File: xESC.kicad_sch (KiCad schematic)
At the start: 48 parts, among them J22 Screw_Terminal_01x03, J36 Conn_02x03_Odd_Even, J39 Screw_Terminal_01x02, J42 Conn_01x02, J45 67800-8005, J48 Conn_01x05, U10 xESC2, U20 2.54mm 2x2 socket, U23 2.54mm 2x2 socket, U26 2.54mm 2x2 socket, U28 LV2862XDDC, U32 2.54mm 1x6 socket, U35 2.54mm 1x6 socket, U38 2.54mm 1x9 socket, U41 2.54mm 1x5 socket

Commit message: Updated to the non-pcb mount xt30 connectors
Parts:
- J42: footprint Connector_AMASS:AMASS_XT30UPB-M_1x02_P5.0mm_Vertical -> Connector_AMASS:AMASS_XT30U-M_1x02_P5.0mm_Vertical; JLC C428721 -> C99101
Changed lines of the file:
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@@
 			)
 		)
-		(property "Footprint" "Connector_AMASS:AMASS_XT30UPB-M_1x02_P5.0mm_Vertical"
+		(property "Footprint" "Connector_AMASS:AMASS_XT30U-M_1x02_P5.0mm_Vertical"
 			(at 224.79 62.23 0)
 			(effects
@@
 			)
 		)
-		(property "JLC" "C428721"
+		(property "JLC" "C99101"
 			(at 224.79 62.23 0)
 			(effects

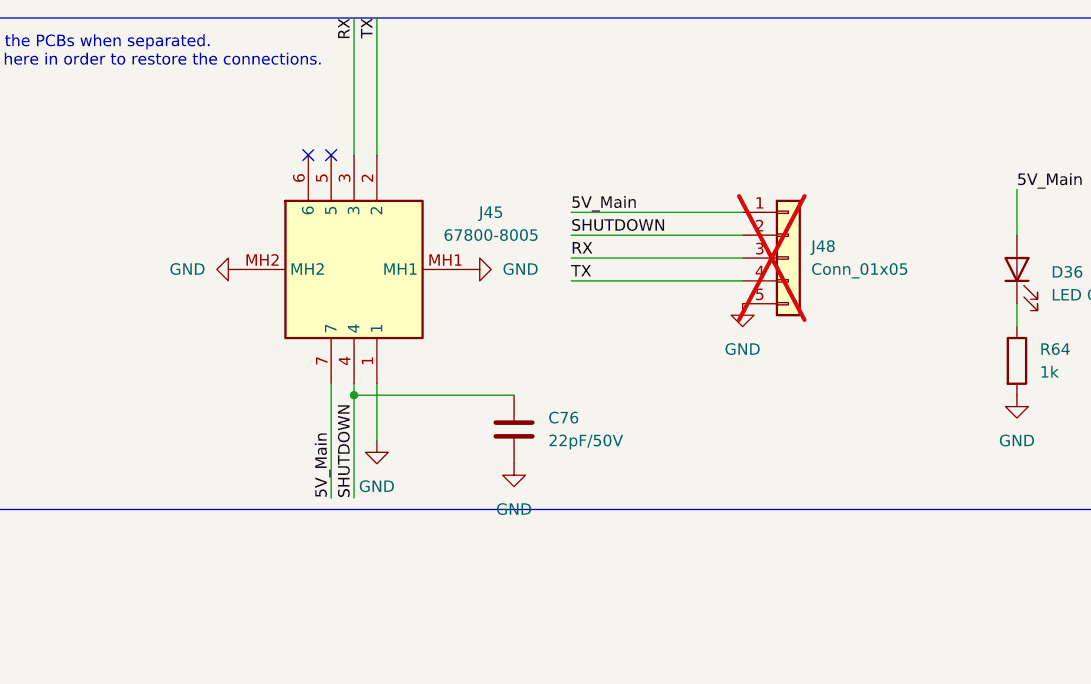
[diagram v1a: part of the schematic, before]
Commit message: Switched SATA to XH connectors
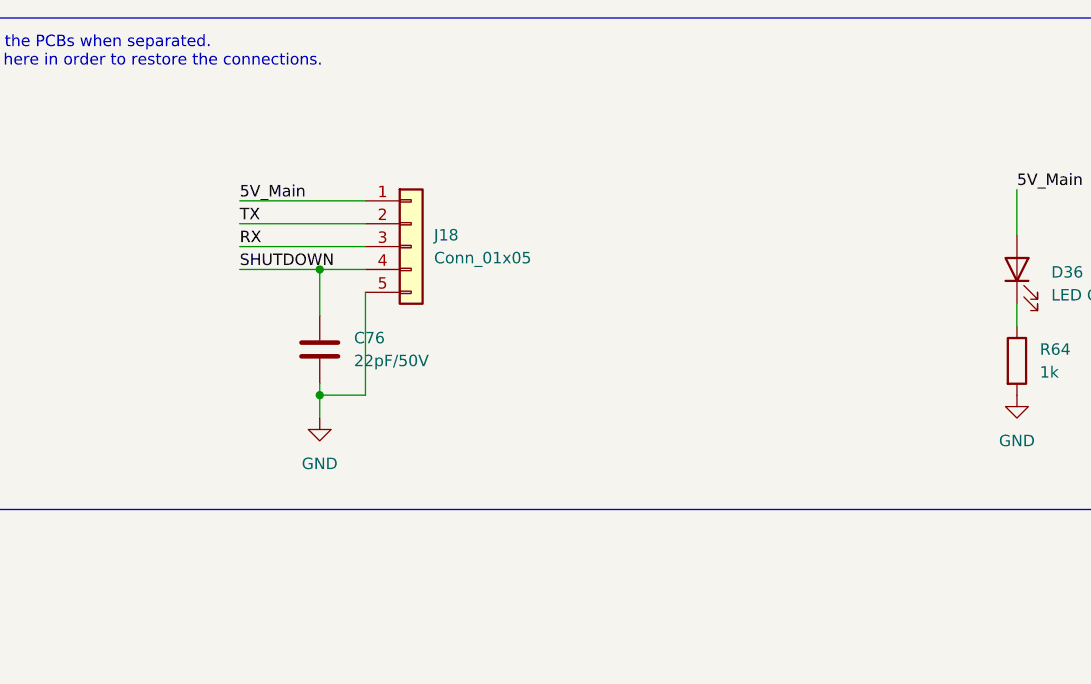
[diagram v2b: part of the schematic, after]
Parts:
- removed J45: 67800-8005, SATA-Molex-67800-8005:SATA-Molex-67800-8005, symbol SATA-Molex-67800-8005:67800-8005
- removed J48: Conn_01x05, Connector_PinHeader_2.54mm:PinHeader_1x05_P2.54mm_Vertical, symbol Connector_Generic:Conn_01x05
- added J18: Conn_01x05, Connector_JST:JST_XH_B5B-XH-A_1x05_P2.50mm_Vertical, symbol Connector_Generic:Conn_01x05
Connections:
- net 5V_Main: now also J18.1 (Pin_1)
- net GND: now also J18.5 (Pin_5)
- net RX: now also J18.3 (Pin_3)
- net SHUTDOWN: now also J18.4 (Pin_4)
- net TX: now also J18.2 (Pin_2)
- no-connect marks 5 -> 3
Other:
- moved on the sheet: C76

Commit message: Fixed BOM
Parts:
- J18: JLC (none) -> C157991
